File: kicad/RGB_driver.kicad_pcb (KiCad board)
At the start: 2 copper layers, 61.4 x 32.6 mm, 17 parts, among them J2 USB_C_Receptacle_USB2.0_16P, SW2 SW_Push_Open_Dual, SW4 SW_Push_Open_Dual, U3 ATtiny85-20P

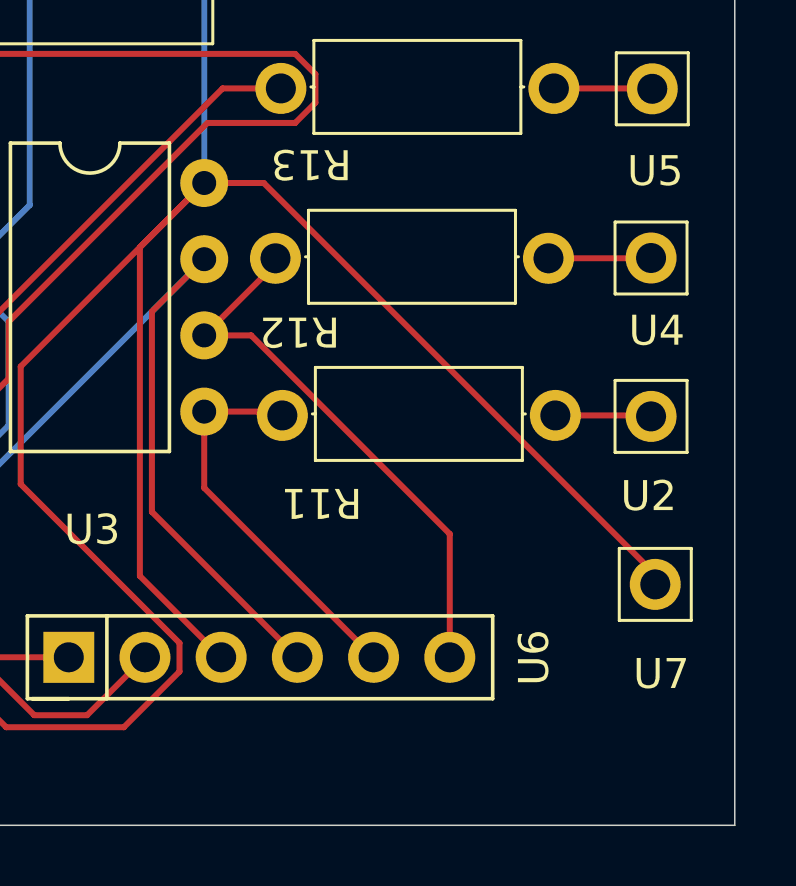
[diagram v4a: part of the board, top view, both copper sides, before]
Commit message: change: external power pad changed to a passive connector, new gerber files
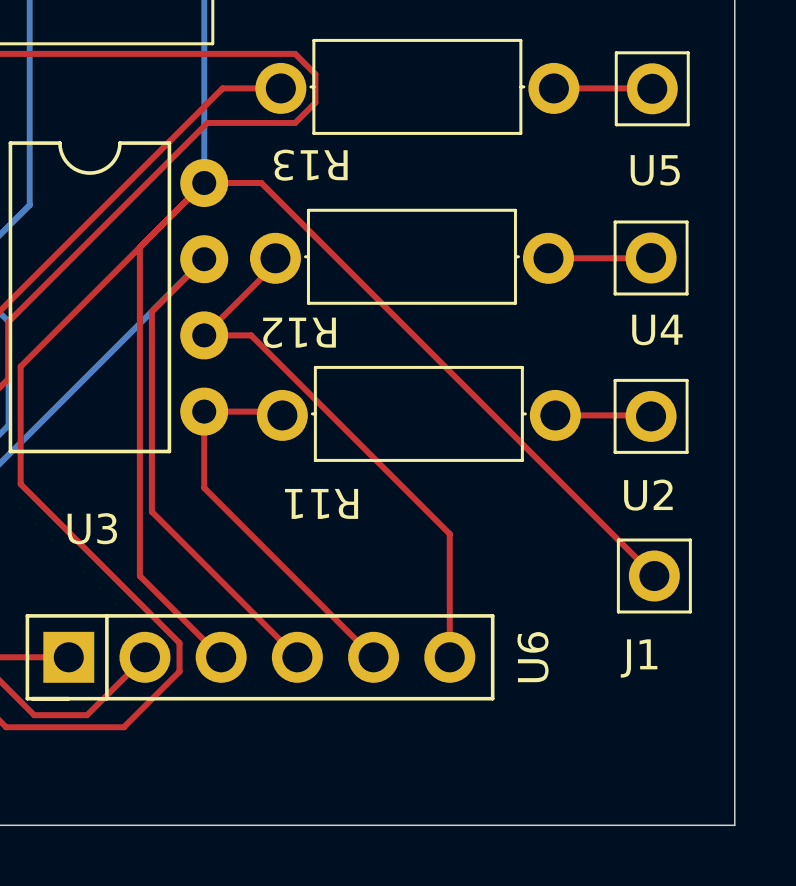
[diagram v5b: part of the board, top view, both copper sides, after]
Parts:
- removed U7: ~, footprint_radiocontorler:simple_generic_pad
- added J1: Conn_01x01_Pin, footprint_radiocontorler:simple_generic_pad, F.Cu at (155.3, 66.8)
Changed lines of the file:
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@@
 	(footprint "footprint_radiocontorler:simple_generic_pad"
 		(layer "F.Cu")
+		(at 155.32 66.79)
+		(property "Reference" "J1"
+			(at -0.41 8.15 0)
+			(unlocked yes)
+			(layer "F.SilkS")
+			(effects
+				(font
+					(size 1 1)
+					(thickness 0.1)
+				)
+			)
+		)
+		(property "Value" "Conn_01x01_Pin"
+			(at 4.23 9.03 0)
+			(unlocked yes)
+			(layer "F.Fab")
+			(effects
+				(font
+					(size 1 1)
+					(thickness 0.15)
+				)
+			)
+		)
+		(property "Datasheet" ""
+			(at 0 0 0)
+			(unlocked yes)
+			(layer "F.Fab")
+			(hide yes)
+			(effects
+				(font
+					(size 1 1)
+					(thickness 0.15)
+				)
+			)
+		)
+		(property "Description" "Generic connector, single row, 01x01, script generated"
+			(at 0 0 0)
+			(unlocked yes)
+			(layer "F.Fab")
+			(hide yes)
+			(effects
+				(font
+					(size 1 1)
+					(thickness 0.15)
+				)
+			)
+		)
+		(property ki_fp_filters "Connector*:*_1x??_*")
+		(sheetname "/")
+		(sheetfile "RGB_driver.kicad_sch")
+		(attr through_hole)
+		(fp_line
+			(start -1.2 4.3)
+			(end 1.2 4.3)
+			(stroke
+				(width 0.1)
+				(type default)
+			)
+			(layer "F.SilkS")
+		)
+		(fp_line
+			(start -1.2 6.7)
+			(end -1.2 4.3)
+			(stroke
+				(width 0.1)
+				(type default)
+			)
+			(layer "F.SilkS")
+		)
+		(fp_line
+			(start 1.2 4.3)
+			(end 1.2 6.7)
+			(stroke
+				(width 0.1)
+				(type default)
+			)
+			(layer "F.SilkS")
+		)
+		(fp_line
+			(start 1.2 6.7)
+			(end -1.2 6.7)
+			(stroke
+				(width 0.1)
+				(type default)
+			)
+			(layer "F.SilkS")
+		)
+		(fp_line
+			(start -1.5 4)
+			(end 1.5 4)
+			(stroke
+				(width 0.05)
+				(type default)
+			)
+			(layer "F.CrtYd")
+		)
+		(fp_line
+			(start -1.5 7)
+			(end -1.5 4)
+			(stroke
+				(width 0.05)
+				(type default)
+			)
+			(layer "F.CrtYd")
+		)
+		(fp_line
+			(start 1.5 4)
+			(end 1.5 7)
+			(stroke
+				(width 0.05)
+				(type default)
+			)
+			(layer "F.CrtYd")
+		)
+		(fp_line
+			(start 1.5 7)
+			(end -1.5 7)
+			(stroke
+				(width 0.05)
+				(type default)
+			)
+			(layer "F.CrtYd")
+		)
+		(fp_line
+			(start -1 4.5)
+			(end -1 6.5)
+			(stroke
+				(width 0.1)
+				(type default)
+			)
+			(layer "F.Fab")
+		)
+		(fp_line
+			(start -1 6.5)
+			(end 1 6.5)
+			(stroke
+				(width 0.1)
+				(type default)
+			)
+			(layer "F.Fab")
+		)
+		(fp_line
+			(start 1 4.5)
+			(end -1 4.5)
+			(stroke
+				(width 0.1)
+				(type default)
+			)
+			(layer "F.Fab")
+		)
+		(fp_line
+			(start 1 6.5)
+			(end 1 4.5)
+			(stroke
+				(width 0.1)
+				(type default)
+			)
+			(layer "F.Fab")
+		)
+		(fp_text user "${REFERENCE}"
+			(at -0.15 8.23 0)
+			(unlocked yes)
+			(layer "F.Fab")
+			(effects
+				(font
+					(size 1 1)
+					(thickness 0.15)
+				)
+			)
+		)
+		(pad "1" thru_hole circle
+			(at 0 5.5)
+			(size 1.7 1.7)
+			(drill 1)
+			(layers "*.Cu" "*.Mask")
+			(remove_unused_layers no)
+			(net 2 "+5V")
+			(pinfunction "Pin_1")
+			(pintype "passive")
+		)
+		(embedded_fonts no)
+	)
+	(footprint "footprint_radiocontorler:simple_generic_pad"
+		(layer "F.Cu")
 		(at 155.21 56.19)
 		(property "Reference" "U4"
@@
 	(footprint "footprint_radiocontorler:simple_generic_pad"
 		(layer "F.Cu")
-		(at 155.35 67.07)
-		(property "Reference" "U7"
-			(at 0.2 8.49 0)
-			(unlocked yes)
-			(layer "F.SilkS")
-			(effects
-				(font
-					(size 1 1)
-					(thickness 0.1)
-				)
-			)
-		)
-		(property "Value" "~"
-			(at -0.04 3.75 0)
-			(unlocked yes)
-			(layer "F.Fab")
-			(effects
-				(font
-					(size 1 1)
-					(thickness 0.15)
-				)
-			)
-		)
-		(property "Datasheet" ""
-			(at 0 0 0)
-			(unlocked yes)
-			(layer "F.Fab")
-			(hide yes)
-			(effects
-				(font
-					(size 1 1)
-					(thickness 0.15)
-				)
-			)
-		)
-		(property "Description" ""
-			(at 0 0 0)
-			(unlocked yes)
-			(layer "F.Fab")
-			(hide yes)
-			(effects
-				(font
-					(size 1 1)
-					(thickness 0.15)
-				)
-			)
-		)
-		(sheetname "/")
-		(sheetfile "RGB_driver.kicad_sch")
-		(attr through_hole)
-		(fp_line
-			(start -1.2 4.3)
-			(end 1.2 4.3)
-			(stroke
-				(width 0.1)
-				(type default)
-			)
-			(layer "F.SilkS")
-		)
-		(fp_line
-			(start -1.2 6.7)
-			(end -1.2 4.3)
-			(stroke
-				(width 0.1)
-				(type default)
-			)
-			(layer "F.SilkS")
-		)
-		(fp_line
-			(start 1.2 4.3)
-			(end 1.2 6.7)
-			(stroke
-				(width 0.1)
-				(type default)
-			)
-			(layer "F.SilkS")
-		)
-		(fp_line
-			(start 1.2 6.7)
-			(end -1.2 6.7)
-			(stroke
-				(width 0.1)
-				(type default)
-			)
-			(layer "F.SilkS")
-		)
-		(fp_line
-			(start -1.5 4)
-			(end 1.5 4)
-			(stroke
-				(width 0.05)
-				(type default)
-			)
-			(layer "F.CrtYd")
-		)
-		(fp_line
-			(start -1.5 7)
-			(end -1.5 4)
-			(stroke
-				(width 0.05)
-				(type default)
-			)
-			(layer "F.CrtYd")
-		)
-		(fp_line
-			(start 1.5 4)
-			(end 1.5 7)
-			(stroke
-				(width 0.05)
-				(type default)
-			)
-			(layer "F.CrtYd")
-		)
-		(fp_line
-			(start 1.5 7)
-			(end -1.5 7)
-			(stroke
-				(width 0.05)
-				(type default)
-			)
-			(layer "F.CrtYd")
-		)
-		(fp_line
-			(start -1 4.5)
-			(end -1 6.5)
-			(stroke
-				(width 0.1)
-				(type default)
-			)
-			(layer "F.Fab")
-		)
-		(fp_line
-			(start -1 6.5)
-			(end 1 6.5)
-			(stroke
-				(width 0.1)
-				(type default)
-			)
-			(layer "F.Fab")
-		)
-		(fp_line
-			(start 1 4.5)
-			(end -1 4.5)
-			(stroke
-				(width 0.1)
-				(type default)
-			)
-			(layer "F.Fab")
-		)
-		(fp_line
-			(start 1 6.5)
-			(end 1 4.5)
-			(stroke
-				(width 0.1)
-				(type default)
-			)
-			(layer "F.Fab")
-		)
-		(fp_text user "${REFERENCE}"
-			(at 0.2 8.49 0)
-			(unlocked yes)
-			(layer "F.Fab")
-			(effects
-				(font
-					(size 1 1)
-					(thickness 0.15)
-				)
-			)
-		)
-		(pad "1" thru_hole circle
-			(at 0 5.5)
-			(size 1.7 1.7)
-			(drill 1)
-			(layers "*.Cu" "*.Mask")
-			(remove_unused_layers no)
-			(net 2 "+5V")
-			(pintype "output")
-		)
-		(embedded_fonts no)
-	)
-	(footprint "footprint_radiocontorler:simple_generic_pad"
-		(layer "F.Cu")
 		(at 155.25 50.55)
 		(property "Reference" "U5"
@@
 	)
 	(segment
+		(start 155.26 72.23)
+		(end 142.22 59.19)
+		(width 0.2)
+		(layer "F.Cu")
+		(net 2)
+	)
+	(segment
 		(start 138.17 61.335)
 		(end 140.315 59.19)
@@
 	)
 	(segment
+		(start 142.22 59.19)
+		(end 140.315 59.19)
+		(width 0.2)
+		(layer "F.Cu")
+		(net 2)
+	)
+	(segment
 		(start 110.559 61.349001)
 		(end 105.129999 55.92)
@@
 	)
 	(segment
-		(start 142.3 59.19)
-		(end 140.315 59.19)
+		(start 155.34 72.23)
+		(end 155.26 72.23)
 		(width 0.2)
 		(layer "F.Cu")
@@
 		(width 0.2)
 		(layer "F.Cu")
-		(net 2)
-	)
-	(segment
-		(start 155.34 72.23)
-		(end 142.3 59.19)
-		(width 0.2)
-		(layer "F.Cu")
